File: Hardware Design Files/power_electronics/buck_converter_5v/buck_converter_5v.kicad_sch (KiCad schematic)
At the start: 16 parts, among them J1 Conn_01x02, J2 Conn_01x02

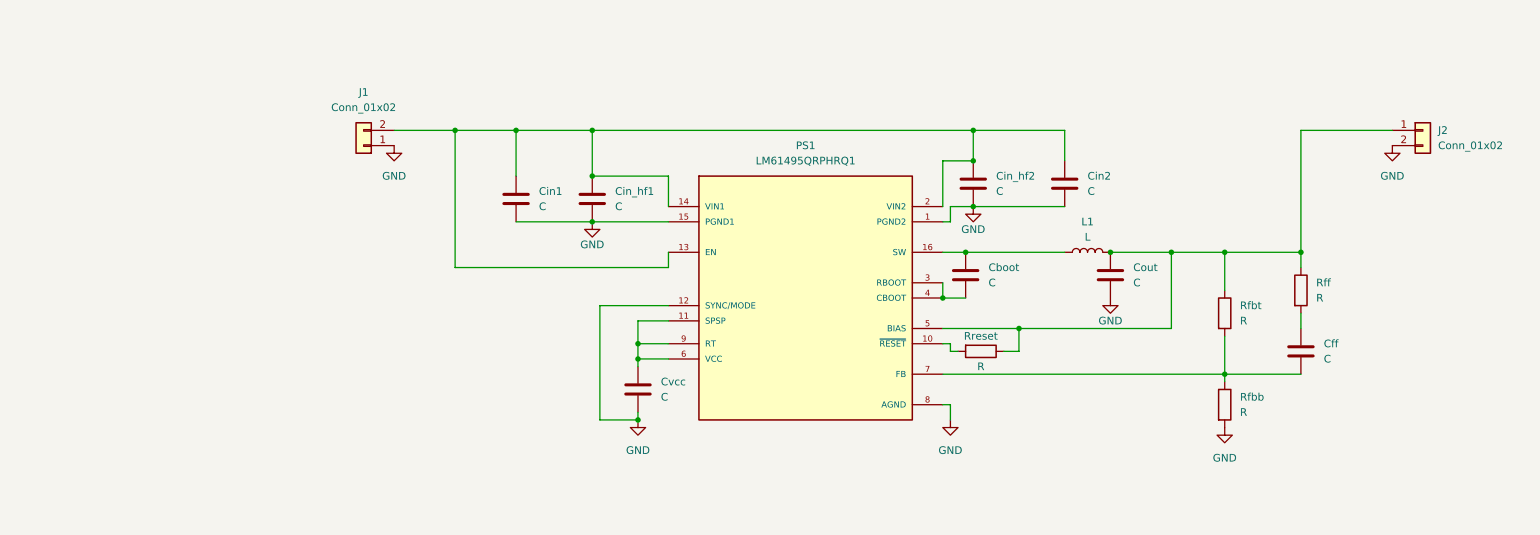
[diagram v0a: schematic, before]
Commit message: feat: apply application ref values to components for block validation doc
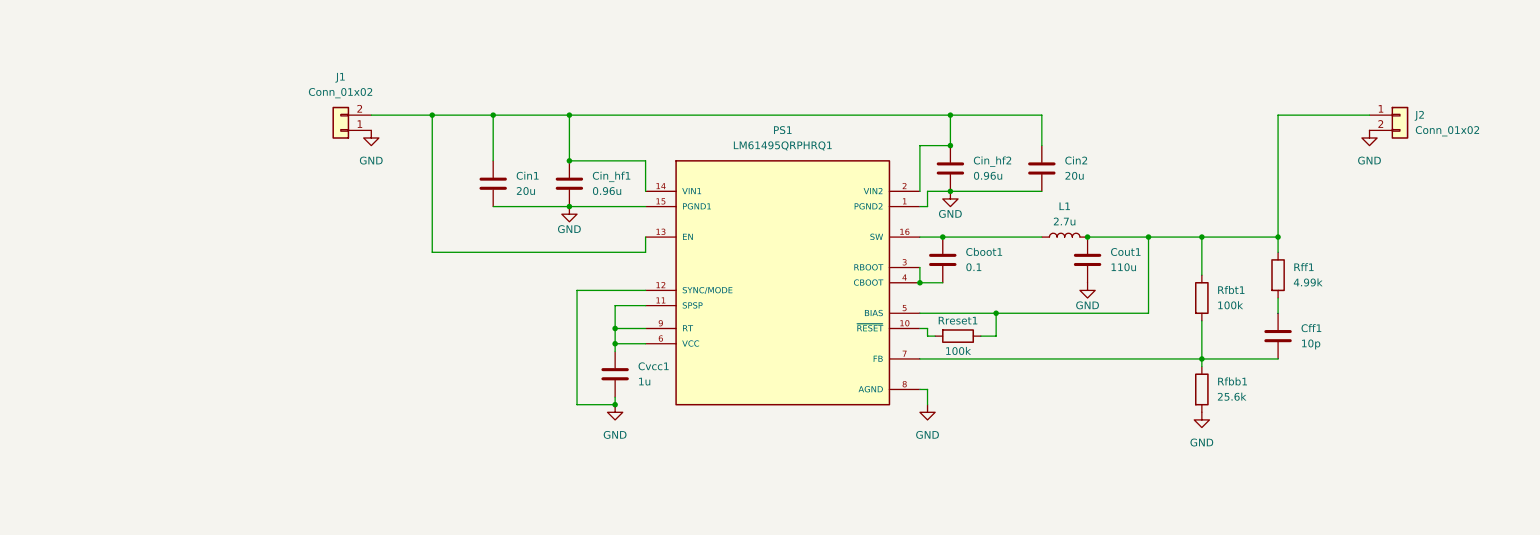
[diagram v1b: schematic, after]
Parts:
- removed Cboot, Cff, Cout, Cvcc: C, symbol Device:C
- removed Rfbb, Rfbt, Rff, Rreset: R, symbol Device:R
- added Cboot1: 0.1, symbol Device:C
- added Cff1: 10p, symbol Device:C
- added Cout1: 110u, symbol Device:C
- added Cvcc1: 1u, symbol Device:C
- added Rfbb1: 25.6k, symbol Device:R
- added Rfbt1, Rreset1: 100k, symbol Device:R
- added Rff1: 4.99k, symbol Device:R
- Cin1, Cin2: value C -> 20u
- Cin_hf1, Cin_hf2: value C -> 0.96u
- L1: value L -> 2.7u
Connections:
- net GND: now also Cout1.2, Cvcc1.1, Rfbb1.2
- net at J2.1 (Pin_1), L1.2, PS1.5 (BIAS): now also Cout1.1, Rfbt1.1, Rff1.1, Rreset1.1
- net at PS1.7 (FB): now also Cff1.2, Rfbb1.1, Rfbt1.2
- net at PS1.10 (~{RESET}): now also Rreset1.2
- net at PS1.11 (SPSP), PS1.6 (VCC), PS1.9 (RT): now also Cvcc1.2
- net at L1.1, PS1.16 (SW): now also Cboot1.1
- net at PS1.3 (RBOOT), PS1.4 (CBOOT): now also Cboot1.2
- new net: Cff1.1, Rff1.2

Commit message: feat(buck_converter): unify pcb design, schematic varies by resistor value, add mounting holes
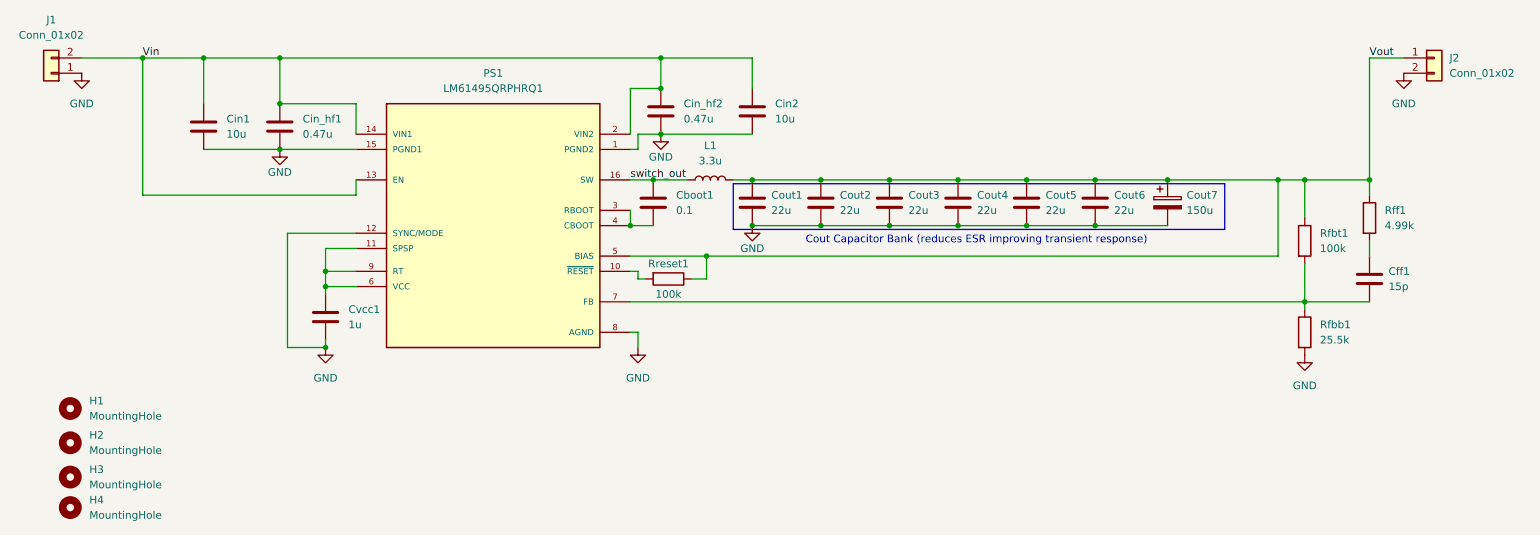
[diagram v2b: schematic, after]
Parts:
- added Cout2, Cout3, Cout4, Cout5, Cout6: 22u, Capacitor_SMD:C_0805_2012Metric, symbol Device:C
- added Cout7: 150u, Capacitor_THT:CP_Radial_D5.0mm_P2.00mm, symbol Device:C_Polarized
- added H1, H2, H3, H4: MountingHole, MountingHole:MountingHole_2.5mm_Pad, symbol Mechanical:MountingHole
- Cboot1: footprint (none) -> Capacitor_SMD:C_0805_2012Metric; Digikey PN (none) -> CL21B104KACNNNC
- Cff1: value 10p -> 15p; footprint (none) -> Capacitor_SMD:C_0805_2012Metric; Digikey PN (none) -> CC0805JRNPO9BN150
- Cin1, Cin2: value 20u -> 10u; footprint (none) -> Capacitor_SMD:C_1206_3216Metric; Digikey PN (none) -> CL31B106KBHNNNE
- Cin_hf1, Cin_hf2: value 0.96u -> 0.47u; footprint (none) -> Capacitor_SMD:C_0603_1608Metric; Digikey PN (none) -> UMK107B7474KA-TR
- Cout1: value 110u -> 22u; footprint (none) -> Capacitor_SMD:C_0805_2012Metric; Digikey PN (none) -> CL21A226MQQNNNE
- Cvcc1: footprint (none) -> Capacitor_SMD:C_0805_2012Metric; Digikey PN (none) -> CL21B105KAFNNNE
- J1, J2: footprint (none) -> custom_footprints:2-terminal-screw-connector-691137710002; Digikey PN (none) -> 691137710002
- L1: value 2.7u -> 3.3u; footprint (none) -> custom_footprints:TMPC 1004H-3R3MG-D; Digikey PN (none) -> TMPC 1004H-3R3MG-D
- PS1: footprint LM61495QRPHRQ1:CONV_LM61495QRPHRQ1 -> custom_footprints:CONV_LM61495QRPHRQ1; Digikey PN (none) -> LM61495QRPHRQ1
- Rfbb1: value 25.6k -> 25.5k; footprint (none) -> Resistor_SMD:R_0805_2012Metric; Digikey PN (none) -> ERA-6AEB2552V
- Rfbt1, Rreset1: footprint (none) -> Resistor_SMD:R_0805_2012Metric; Digikey PN (none) -> ERA-6AEB104V
- Rff1: footprint (none) -> Resistor_SMD:R_0805_2012Metric; Digikey PN (none) -> ERA-6AEB4991V
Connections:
- net GND: now also Cout2.2, Cout3.2, Cout4.2, Cout5.2, Cout6.2, Cout7.2
- net Vin: now reaches Cin1.1, Cin2.1, Cin_hf1.1, Cin_hf2.1, J1.2 (Pin_2), PS1.13 (EN), PS1.14 (VIN1), PS1.2 (VIN2)
- net switch_out: now reaches Cboot1.1, L1.1, PS1.16 (SW)
- net Vout: now reaches Cout1.1, J2.1 (Pin_1), L1.2, PS1.5 (BIAS), Rfbt1.1, Rff1.1, Rreset1.1
- net Vout: now also Cout2.1, Cout3.1, Cout4.1, Cout5.1, Cout6.1, Cout7.1
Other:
- note added: "Cout Capacitor Bank (reduces ESR improving transient response)"
